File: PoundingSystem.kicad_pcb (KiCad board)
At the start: 4 copper layers, 184.2 x 37.8 mm, 139 parts, among them J1 USB_B_Micro, J2 LINE OUT, J3 MICROPHONE, J4 LINE IN, J5 HEADPHONES, J6 Debug, SW1 Rotary_Encoder_Switch, SW2 Rotary_Encoder, SW3 Rotary_Encoder, SW4 Rotary_Encoder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

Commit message: h7 version;
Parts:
- removed C10, C11, C28, C36, C39, C40, C53: 100nf, Capacitor_SMD:C_0402_1005Metric
- removed C50: 10nf, Capacitor_SMD:C_0402_1005Metric
- removed G***: LOGO, Libraries:PoundingSystemLogo
- removed R28: 10k, Resistor_SMD:R_0402_1005Metric
- removed SW6: SW_SPST, Button_Switch_THT:SW_PUSH_6mm_H4.3mm
- removed U12, U4, U6, U8, U9: SN74LVC2G34, Package_TO_SOT_SMD:SOT-23-6
- added C58: 4.7u, Capacitor_SMD:C_0603_1608Metric, F.Cu at (181.6, 80.4)
- added C59: 100nf, Capacitor_SMD:C_0402_1005Metric, F.Cu at (187.9, 97.4)
- added C60: 100nf, Capacitor_SMD:C_0402_1005Metric, F.Cu at (166.6, 108.9)
- added C61: 100nf, Capacitor_SMD:C_0402_1005Metric, F.Cu at (175.3, 76.3)
- added C62: 100nf, Capacitor_SMD:C_0402_1005Metric, F.Cu at (182.9, 102.3)
- added C63: 100nf, Capacitor_SMD:C_0402_1005Metric, F.Cu at (175.9, 109.9)
- added C64: 100nf, Capacitor_SMD:C_0402_1005Metric, F.Cu at (180.5, 81.5)
- added C65: 100nf, Capacitor_SMD:C_0402_1005Metric, F.Cu at (178.9, 106.1)
- added C66: 100nf, Capacitor_SMD:C_0402_1005Metric, F.Cu at (188.6, 89.6)
- added C67: 100nf, Capacitor_SMD:C_0402_1005Metric, F.Cu at (184.1, 85.0)
- added D8: LED_BPM, LED_SMD:LED_0805_2012Metric, B.Cu at (204.7, 80.4)
- added R34: 10k, Resistor_SMD:R_0402_1005Metric, F.Cu at (41.6, 80.5)
- added R35: 10k, Resistor_SMD:R_0402_1005Metric, F.Cu at (48.8, 103.8)
- added R36: 0, Resistor_SMD:R_0402_1005Metric, F.Cu at (155.7, 85.9)
- added R37: 10k, Resistor_SMD:R_0402_1005Metric, F.Cu at (183.5, 76.8)
- added U13: STM32H743IITx, Package_QFP:LQFP-176_24x24mm_P0.5mm, F.Cu at (171.6, 93.0)
- C3: value 10u -> 100nf; footprint Capacitor_SMD:C_0603_1608Metric -> Capacitor_SMD:C_0402_1005Metric
- R5: value 2k2 -> 10k
- R6: value 2k2 -> 180; footprint Resistor_SMD:R_0402_1005Metric -> Resistor_SMD:R_0603_1608Metric
- U2: value STM32F405RGT6 -> CAT24C256; footprint Package_QFP:LQFP-64_10x10mm_P0.5mm -> Package_SO:SOIC-8-1EP_3.9x4.9mm_P1.27mm_EP2.29x3mm
- moved R5 42.9 mm to (205.9, 90.0), turned to 0 degrees
- moved R6 41.6 mm to (202.8, 82.8), turned to 180 degrees
- moved C9 36.8 mm to (200.2, 81.8), turned to 90 degrees
- moved U2 29.2 mm to (196.5, 79.8), turned to 270 degrees
- moved C18 23.7 mm to (154.8, 79.2), turned to 90 degrees
- moved HSE1 23.5 mm to (157.9, 79.2), turned to 180 degrees
- moved C17 23.5 mm to (160.8, 79.2), turned to 270 degrees
- moved D1 23.0 mm to (214.6, 100.8), turned to 90 degrees
- moved C12 22.7 mm to (157.0, 86.9), turned to 45 degrees
- moved C3 22.4 mm to (159.5, 101.4)
- moved C8 21.5 mm to (161.3, 82.8), turned to 225 degrees
- moved R2 21.4 mm to (157.4, 82.0), turned to 90 degrees
- moved J6 21.3 mm to (214.6, 95.6), turned to 0 degrees
- moved C13 20.9 mm to (154.8, 88.7), turned to 225 degrees
- moved FB2 20.9 mm to (153.9, 84.2), turned to 90 degrees
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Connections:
- C12 pad 1: +3V3 -> GND
- C12 pad 2: GND -> +3V3
- C3 pad 1: +3V3 -> GND
- C3 pad 2: GND -> +3V3
- C4 pad 1: +3V3 -> GND
- C4 pad 2: GND -> +3V3
- C5 pad 1: +3V3 -> GND
- C5 pad 2: GND -> +3V3
- C6 pad 1: +3V3 -> GND
- C6 pad 2: GND -> +3V3
- C7 pad 1: +3V3 -> GND
- C7 pad 2: GND -> +3V3
- C8 pad 1: +3V3 -> GND
- C8 pad 2: GND -> +3V3
- R15 pad 2: LCD_BL -> LCD_BL1
- R16 pad 2: LCD_BL -> LCD_BL2
- R17 pad 1: Net-(R17-Pad1) -> TIM3_CH2
- R18 pad 1: Net-(R18-Pad1) -> TIM3_CH1
- R19 pad 1: Net-(R19-Pad1) -> TIM1_CH1
- R20 pad 1: Net-(R20-Pad1) -> TIM1_CH2
- R21 pad 1: Net-(R21-Pad1) -> TIM5_CH2
- R22 pad 1: Net-(R22-Pad1) -> TIM4_CH2
- R23 pad 1: Net-(R23-Pad1) -> TIM5_CH1
- R24 pad 1: Net-(R24-Pad1) -> TIM4_CH1
- R29 pad 1: Net-(R29-Pad1) -> SW1_A
- R3 pad 2: LCD_BL -> LCD_BL2
- R30 pad 1: Net-(R30-Pad1) -> SW1_B
- R4 pad 2: LCD_BL -> LCD_BL1
- R5 pad 1: +3V3 -> Net-(C49-Pad2)
- R5 pad 2: I2C2_SCL -> +3V3
- R6 pad 1: +3V3 -> Net-(D8-Pad2)
- R6 pad 2: I2C2_SDA -> LED_BPM
- SW9 pad 1: Net-(D2-Pad2) -> Net-(SW9-Pad1)
- SW9 pad 2: +5V -> Net-(D2-Pad2)
- SW9 pad 3: Net-(SW9-Pad3) -> +5V
- U11 pad 4: BACK_BTN -> Net-(U11-Pad4)
- U2 pad 1: +3V3 -> GND
- U2 pad 2: SW1_B -> GND
- U2 pad 3: SW1_A -> GND
- U2 pad 4: SW1_BTN -> GND
- U2 pad 5: HSE_IN -> I2C1_SDA
- U2 pad 6: HSE_OUT -> I2C1_SCL
- U2 pad 7: NRST -> EEP_WP
- U2 pad 8: Net-(U2-Pad8) -> +3V3
- U2 pad 9: Net-(U2-Pad9) -> (no net)
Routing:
- net TIM2_CH1: track 89.8 -> 0.00 mm, vias 2 -> 0
- net TIM2_CH2: track 88.1 -> 0.00 mm, vias 2 -> 0
- net TIM5_CH2: track 0.00 -> 87.7 mm, vias 0 -> 2
- net TIM5_CH1: track 0.00 -> 78.8 mm, vias 0 -> 2
- net LCD_BL: track 78.7 -> 0.00 mm, vias 5 -> 0
- net +3V3: track 97.0 -> 129.1 mm, vias 24 -> 32
- net BACK_BTN: track 28.2 -> 0.00 mm, vias 2 -> 0
- net USB_D-: track 39.5 -> 67.4 mm, vias 2 -> 4
- net LCD_BL2: track 0.00 -> 25.6 mm, vias 0 -> 3
- net USB_D+: track 37.3 -> 62.1 mm
- net I2C1_SCL: track 0.00 -> 22.7 mm
- net I2C1_SDA: track 0.00 -> 21.6 mm
- net LED_BPM: track 0.00 -> 19.7 mm
- net SPI3_SCK: track 23.7 -> 4.16 mm
- net LCD_BL1: track 0.00 -> 18.4 mm
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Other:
- net class Default: clearance 0.254 -> 0.2
- rule trace_clearance: 0.254 -> 0.2

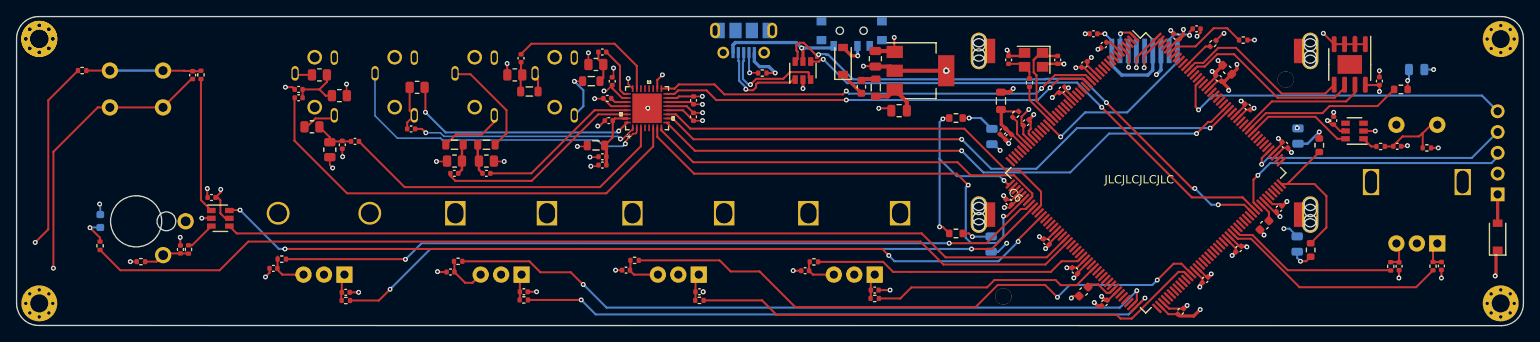
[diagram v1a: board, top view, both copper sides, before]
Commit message: switch MPU to stm32h7
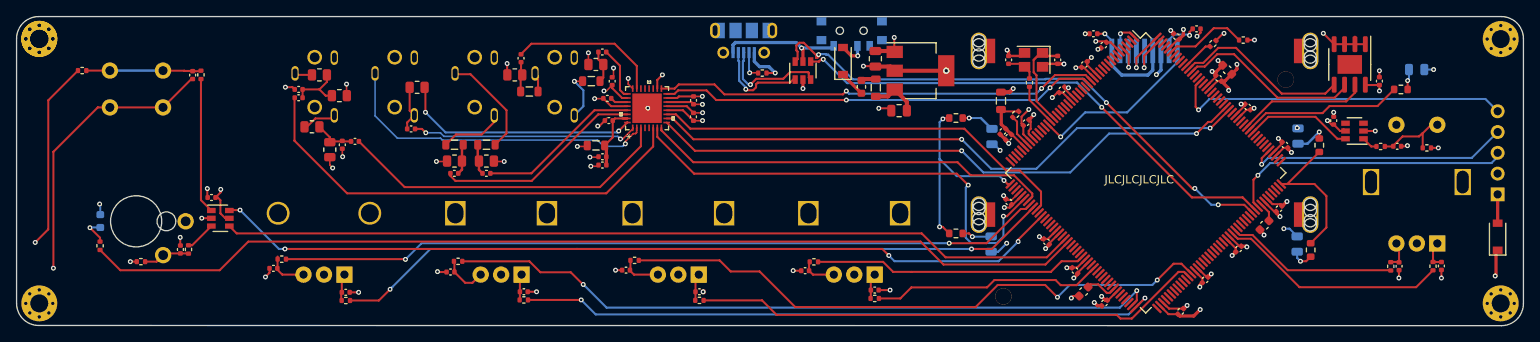
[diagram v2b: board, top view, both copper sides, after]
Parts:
- added G***: LOGO, Logo`:PoundingSystemLogo, B.Cu at (126.0, 83.8)
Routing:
- net +3V3: track 129.1 -> 130.3 mm, vias 32 -> 33

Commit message: production: generate production files
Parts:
- removed the G*** at (126.0, 83.8)
- added G***: LOGO, Logo:PoundingSystemLogo, B.Cu at (126.2, 84.0)
- U10, U11: footprint Package_TO_SOT_SMD:SOT-23-6 -> Package_TO_SOT_SMD:SOT-363_SC-70-6

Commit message: fix: update schematic labels
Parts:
- removed G***: LOGO, Logo:PoundingSystemLogo
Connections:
- net SPI3_MOSI renamed SPI4_MOSI
- net SPI3_SCK renamed SPI4_SCK
